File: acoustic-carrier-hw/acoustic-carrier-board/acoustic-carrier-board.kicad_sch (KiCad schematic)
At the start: 0 parts

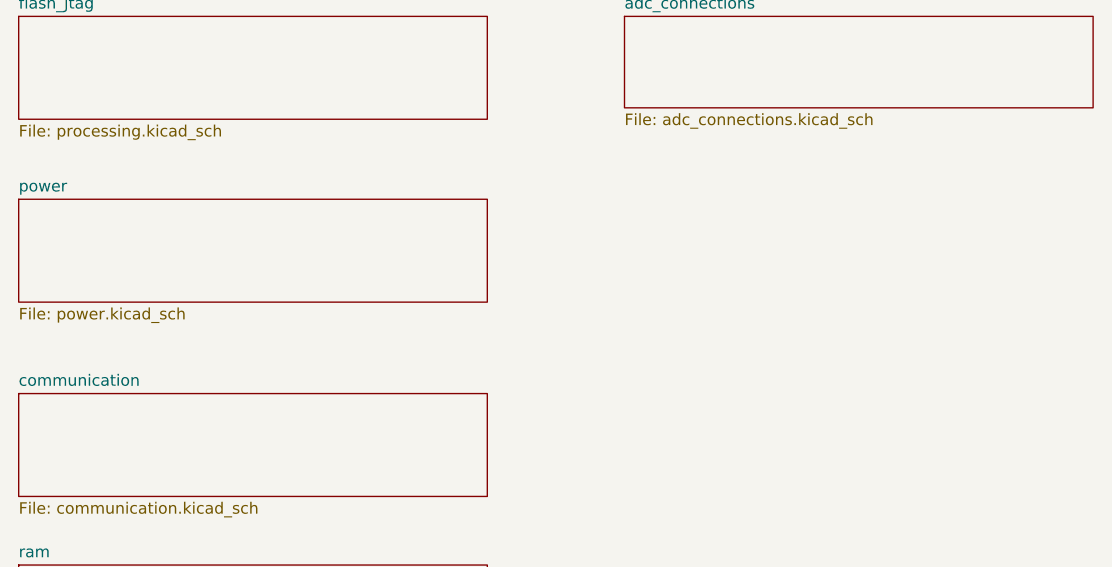
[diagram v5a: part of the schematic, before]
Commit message: [carrier] Checked ethernet decoupling + pins + pad + resonator
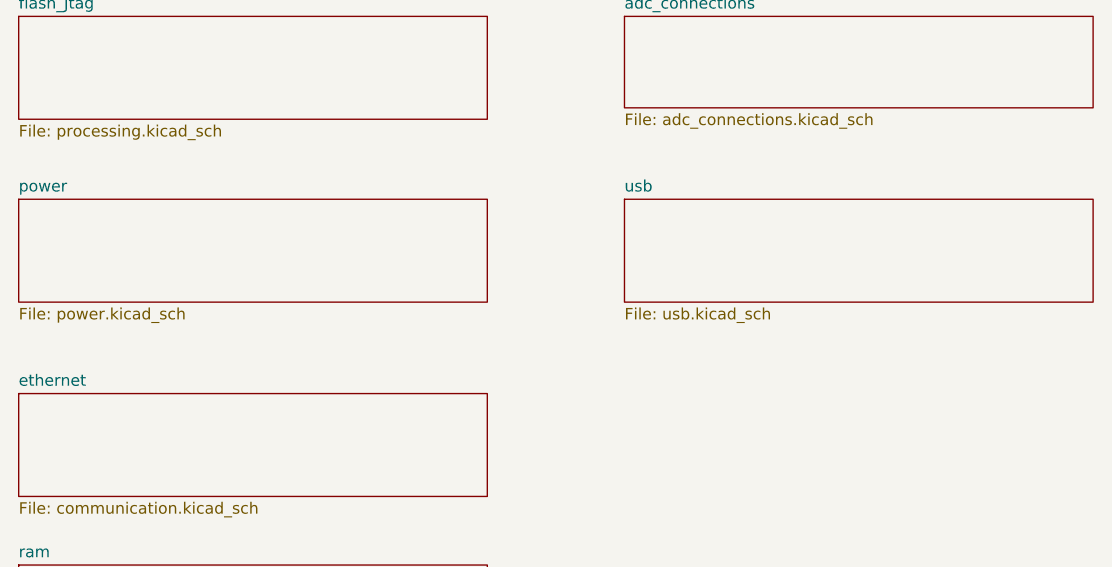
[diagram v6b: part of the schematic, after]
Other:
- sheet communication renamed ethernet
- added sheet usb (usb.kicad_sch)
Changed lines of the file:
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@@
 			(project "acoustic-carrier-board"
 				(path "/25b015c9-ab13-4427-b72c-b6f348597100"
-					(page "8")
+					(page "9")
+				)
+			)
+		)
+	)
+	(sheet
+		(at 82.55 64.77)
+		(size 52.07 11.43)
+		(exclude_from_sim no)
+		(in_bom yes)
+		(on_board yes)
+		(dnp no)
+		(fields_autoplaced yes)
+		(stroke
+			(width 0.1524)
+			(type solid)
+		)
+		(fill
+			(color 0 0 0 0.0000)
+		)
+		(property "Sheetname" "usb"
+			(at 82.55 64.0584 0)
+			(effects
+				(font
+					(size 1.27 1.27)
+				)
+				(justify left bottom)
+			)
+		)
+		(property "Sheetfile" "usb.kicad_sch"
+			(at 82.55 76.7846 0)
+			(effects
+				(font
+					(size 1.27 1.27)
+				)
+				(justify left top)
+			)
+		)
+		(instances
+			(project "acoustic-carrier-board"
+				(path "/25b015c9-ab13-4427-b72c-b6f348597100"
+					(page "7")
 				)
 			)
@@
 			(color 0 0 0 0.0000)
 		)
-		(property "Sheetname" "communication"
+		(property "Sheetname" "ethernet"
 			(at 15.24 85.6484 0)
 			(effects
@@
 			(project "acoustic-carrier-board"
 				(path "/25b015c9-ab13-4427-b72c-b6f348597100"
-					(page "7")
+					(page "8")
 				)
 			)

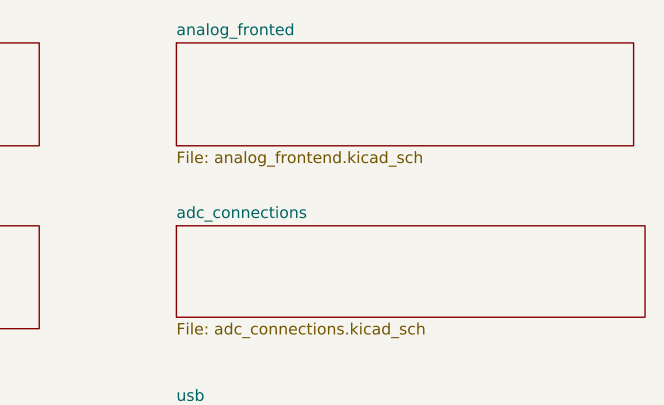
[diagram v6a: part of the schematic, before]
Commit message: [carrier] Reorganized schematic, moPut adc signals in bus, fixed DRC errors (next) recheck ethernet, check usb, add power switch
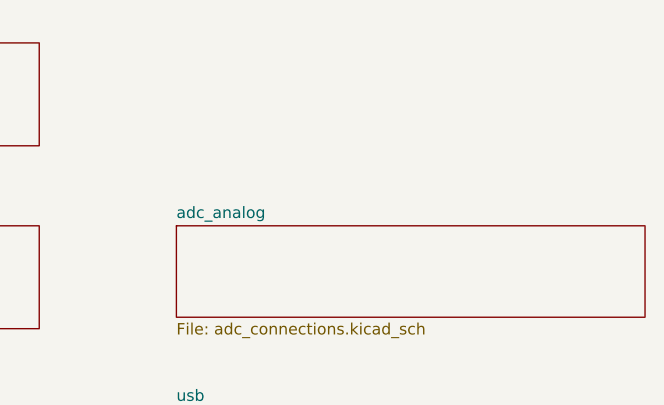
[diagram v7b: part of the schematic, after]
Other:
- sheet adc_connections renamed adc_analog
- removed sheet analog_fronted
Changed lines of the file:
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@@
 	(paper "A4")
-	(sheet
-		(at 82.55 24.13)
-		(size 50.8 11.43)
-		(exclude_from_sim no)
-		(in_bom yes)
-		(on_board yes)
-		(dnp no)
-		(fields_autoplaced yes)
-		(stroke
-			(width 0.1524)
-			(type solid)
-		)
-		(fill
-			(color 0 0 0 0.0000)
-		)
-		(property "Sheetname" "analog_fronted"
-			(at 82.55 23.4184 0)
-			(effects
-				(font
-					(size 1.27 1.27)
-				)
-				(justify left bottom)
-			)
-		)
-		(property "Sheetfile" "analog_frontend.kicad_sch"
-			(at 82.55 36.1446 0)
-			(effects
-				(font
-					(size 1.27 1.27)
-				)
-				(justify left top)
-			)
-		)
-		(instances
-			(project "acoustic-carrier-board"
-				(path "/25b015c9-ab13-4427-b72c-b6f348597100"
-					(page "3")
-				)
-			)
-		)
-	)
 	(sheet
 		(at 15.24 44.45)
@@
 			(color 0 0 0 0.0000)
 		)
-		(property "Sheetname" "adc_connections"
+		(property "Sheetname" "adc_analog"
 			(at 82.55 43.7384 0)
 			(effects
@@
 			(project "acoustic-carrier-board"
 				(path "/25b015c9-ab13-4427-b72c-b6f348597100"
-					(page "9")
+					(page "10")
 				)
 			)
@@
 			(project "acoustic-carrier-board"
 				(path "/25b015c9-ab13-4427-b72c-b6f348597100"
-					(page "8")
-				)
-			)
+					(page "3")
+				)
+			)

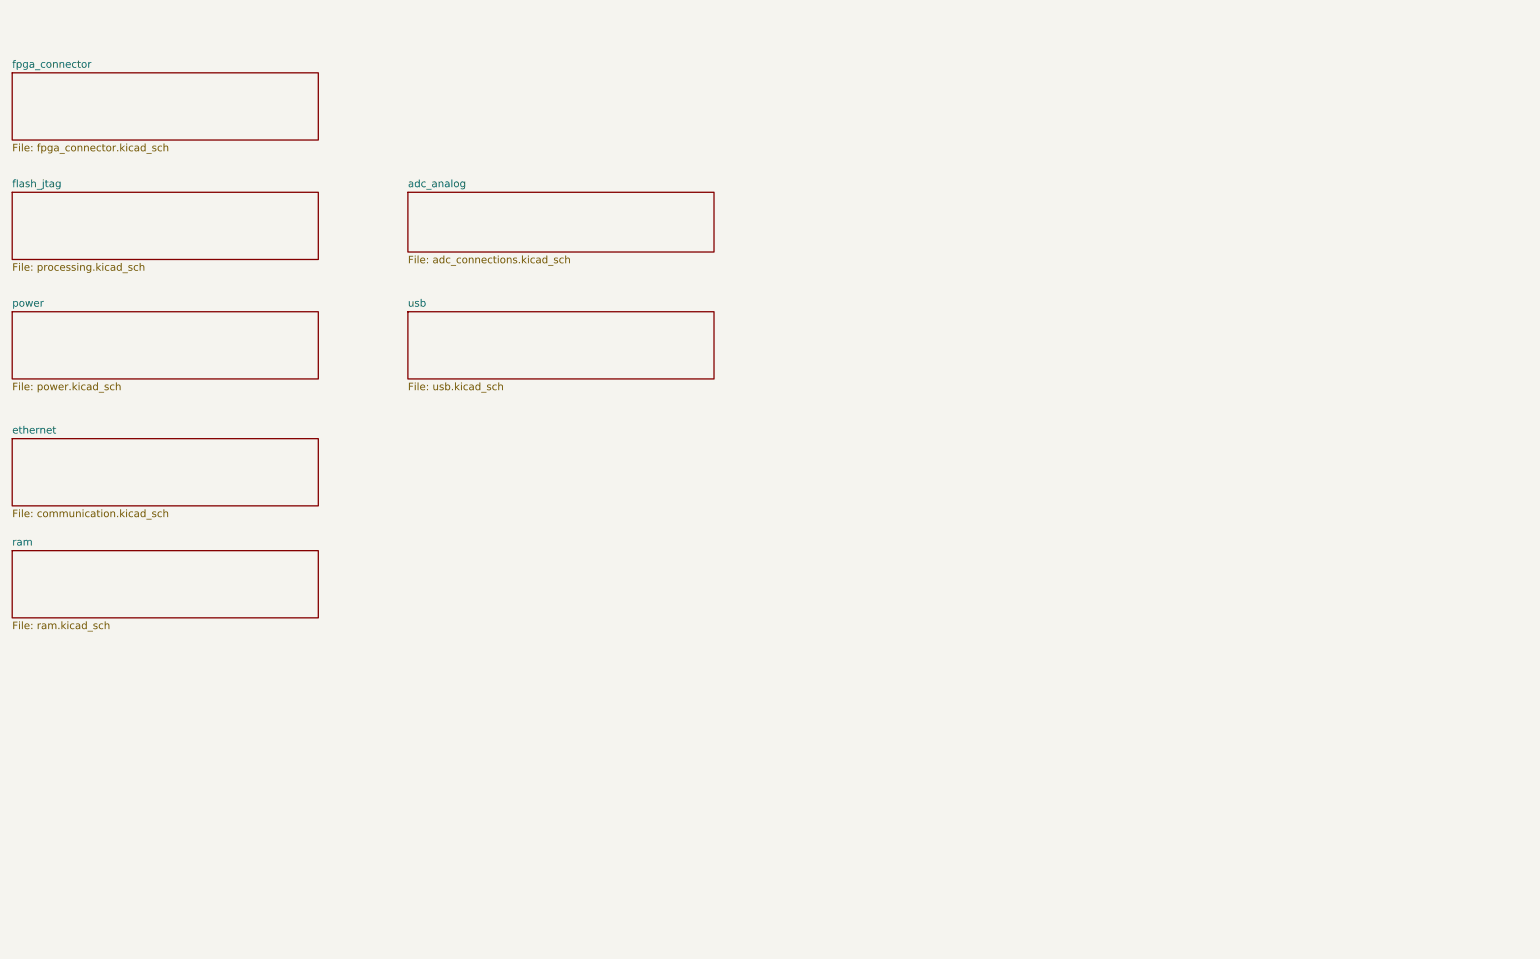
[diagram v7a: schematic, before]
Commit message: [carrier] Signal switch-around in ddr3
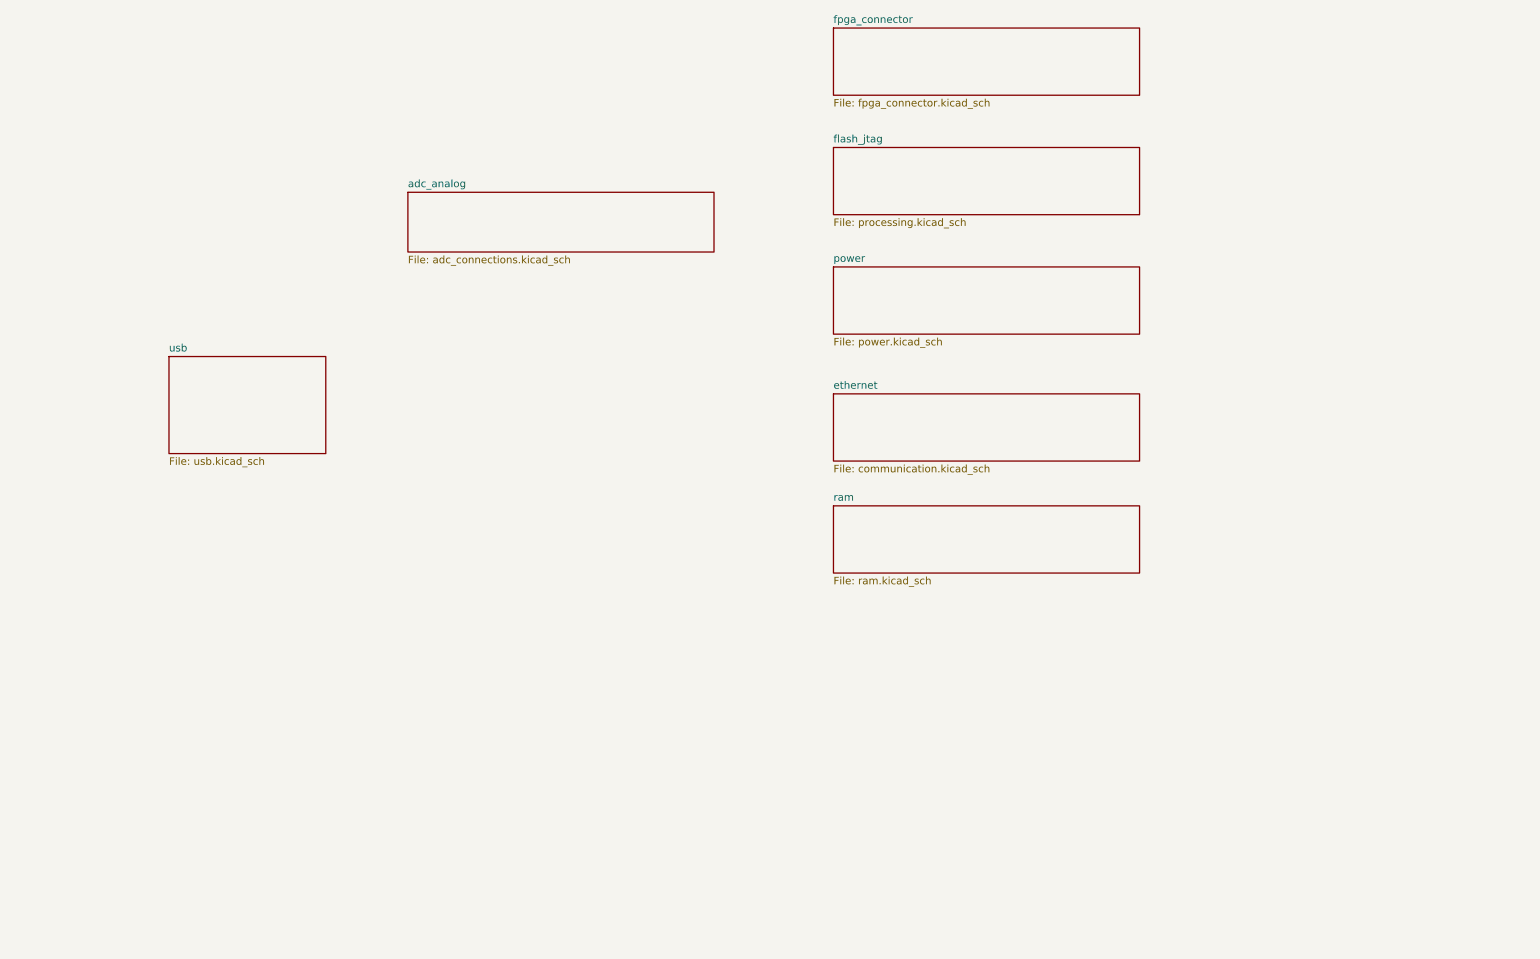
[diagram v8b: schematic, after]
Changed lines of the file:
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@@
 	(paper "A4")
 	(sheet
-		(at 15.24 44.45)
+		(at 154.94 36.83)
 		(size 52.07 11.43)
 		(exclude_from_sim no)
@@
 		)
 		(property "Sheetname" "flash_jtag"
-			(at 15.24 43.7384 0)
+			(at 154.94 36.1184 0)
 			(effects
 				(font
@@
 		)
 		(property "Sheetfile" "processing.kicad_sch"
-			(at 15.24 56.4646 0)
+			(at 154.94 48.8446 0)
 			(effects
 				(font
@@
 	)
 	(sheet
-		(at 15.24 64.77)
+		(at 154.94 57.15)
 		(size 52.07 11.43)
 		(exclude_from_sim no)
@@
 		)
 		(property "Sheetname" "power"
-			(at 15.24 64.0584 0)
+			(at 154.94 56.4384 0)
 			(effects
 				(font
@@
 		)
 		(property "Sheetfile" "power.kicad_sch"
-			(at 15.24 76.7846 0)
+			(at 154.94 69.1646 0)
 			(effects
 				(font
@@
 		)
 		(property "Field2" ""
-			(at 15.24 64.77 0)
+			(at 154.94 57.15 0)
 			(effects
 				(font
@@
 	)
 	(sheet
-		(at 15.24 24.13)
+		(at 154.94 16.51)
 		(size 52.07 11.43)
 		(exclude_from_sim no)
@@
 		)
 		(property "Sheetname" "fpga_connector"
-			(at 15.24 23.4184 0)
+			(at 154.94 15.7984 0)
 			(effects
 				(font
@@
 		)
 		(property "Sheetfile" "fpga_connector.kicad_sch"
-			(at 15.24 36.1446 0)
+			(at 154.94 28.5246 0)
 			(effects
 				(font
@@
 	)
 	(sheet
-		(at 82.55 64.77)
-		(size 52.07 11.43)
+		(at 41.91 72.39)
+		(size 26.67 16.51)
 		(exclude_from_sim no)
 		(in_bom yes)
@@
 		)
 		(property "Sheetname" "usb"
-			(at 82.55 64.0584 0)
+			(at 41.91 71.6784 0)
 			(effects
 				(font
@@
 		)
 		(property "Sheetfile" "usb.kicad_sch"
-			(at 82.55 76.7846 0)
+			(at 41.91 89.4846 0)
 			(effects
 				(font
@@
 	)
 	(sheet
-		(at 15.24 86.36)
+		(at 154.94 78.74)
 		(size 52.07 11.43)
 		(exclude_from_sim no)
@@
 		)
 		(property "Sheetname" "ethernet"
-			(at 15.24 85.6484 0)
+			(at 154.94 78.0284 0)
 			(effects
 				(font
@@
 		)
 		(property "Sheetfile" "communication.kicad_sch"
-			(at 15.24 98.3746 0)
+			(at 154.94 90.7546 0)
 			(effects
 				(font
@@
 		)
 		(property "Field2" ""
-			(at 15.24 86.36 0)
+			(at 154.94 78.74 0)
 			(effects
 				(font
@@
 	)
 	(sheet
-		(at 15.24 105.41)
+		(at 154.94 97.79)
 		(size 52.07 11.43)
 		(exclude_from_sim no)
@@
 		)
 		(property "Sheetname" "ram"
-			(at 15.24 104.6984 0)
+			(at 154.94 97.0784 0)
 			(effects
 				(font
@@
 		)
 		(property "Sheetfile" "ram.kicad_sch"
-			(at 15.24 117.4246 0)
+			(at 154.94 109.8046 0)
 			(effects
 				(font
@@
 		)
 		(property "Field2" ""
-			(at 15.24 105.41 0)
-			(effects
-				(font
+			(at 154.94 97.79 0)
+			(effects
+				(font
